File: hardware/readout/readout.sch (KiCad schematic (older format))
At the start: 0 parts

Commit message: Schematic progress
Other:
- note added: "Each sheet represents\n6 CITIROC ASICS\neach processing 32 SiPMs"
- note added: "Each sheet represents\nOne Trenz FPGA module\nprocessing 96 SiPMs"
- note added: "Each sheet represents\ntwo backplane connectors\ncarrying 192 SiPM inputs"
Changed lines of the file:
@@
 $Descr A4 11693 8268
 encoding utf-8
-Sheet 1 9
+Sheet 1 12
 Title ""
 Date ""
@@
 EMPHATIC Readout Board
 $Sheet
-S 1050 950  1000 1000
-U 61016FDD
-F0 "96Chan.sch" 50
-F1 "96Chan.sch" 50
-F2 "TRIG[0..95]" O R 2050 1450 50
+S 1400 2000 1050 700
+U 61195331
+F0 "sheet61195329" 50
+F1 "bp192.sch" 50
+F2 "SIPM[0..191]" O R 2450 2150 50
+F3 "VDD" I L 1400 2150 50
+F4 "BIAS[1..12]" I L 1400 2450 50
+F5 "TEMP[1..4]" O R 2450 2450 50
 $EndSheet
 $Sheet
-S 2750 950  750  1000
-U 61042CB4
-F0 "trenz" 50
+S 1400 3150 1050 700
+U 61195337
+F0 "sheet6119532A" 50
+F1 "bp192.sch" 50
+F2 "SIPM[0..191]" O R 2450 3300 50
+F3 "VDD" I L 1400 3300 50
+F4 "BIAS[1..12]" I L 1400 3600 50
+F5 "TEMP[1..4]" O R 2450 3600 50
+$EndSheet
+$Sheet
+S 1400 4300 1050 700
+U 6119533D
+F0 "sheet6119532B" 50
+F1 "bp192.sch" 50
+F2 "SIPM[0..191]" O R 2450 4450 50
+F3 "VDD" I L 1400 4450 50
+F4 "BIAS[1..12]" I L 1400 4750 50
+F5 "TEMP[1..4]" O R 2450 4750 50
+$EndSheet
+$Sheet
+S 4950 1800 1250 700
+U 611955AA
+F0 "sheet611955AA" 50
 F1 "trenz.sch" 50
-F2 "TRIG[0..95]" I L 2750 1450 50
-F3 "DATA_TX_P" O R 3500 1100 50
-F4 "DATA_TX_N" O R 3500 1200 50
-F5 "DATA_RX_P" I R 3500 1650 50
-F6 "DATA_RX_N" I R 3500 1750 50
+F2 "TRIG[0..95]" I L 4950 2150 50
+F3 "DATA_TX_P" O R 6200 1950 50
+F4 "DATA_TX_N" O R 6200 2050 50
+F5 "DATA_RX_P" I R 6200 2250 50
+F6 "DATA_RX_N" I R 6200 2350 50
+$EndSheet
+$Sheet
+S 3150 2000 1200 700
+U 61098CF8
+F0 "6xCITIROC" 50
+F1 "18xCITIROC.sch" 50
+F2 "SIPM[0..191]" I L 3150 2150 50
+F3 "TRIG[0..95]" O R 4350 2150 50
+F4 "TRIG[96..191]" O R 4350 2600 50
+F5 "CCTRL[0..4]" I L 3150 2350 50
+F6 "APROBE[0..5]" O R 4350 2300 50
+F7 "DPROBE[0..5]" O R 4350 2450 50
+F8 "SRCLK[0..5]" I L 3150 2500 50
 $EndSheet
 Wire Bus Line
-	2750 1450 2050 1450
-Text Label 2200 1450 0    50   ~ 0
-TRIG[0..95]
+	2450 2150 3150 2150
+Text Label 2550 2150 0    50   ~ 0
+SIPM[0..191]
+Text Notes 1150 1300 0    75   ~ 0
+Each sheet represents\ntwo backplane connectors\ncarrying 192 SiPM inputs
+Text Notes 3050 1250 0    75   ~ 0
+Each sheet represents\n6 CITIROC ASICS\neach processing 32 SiPMs
+Text Notes 6100 1200 0    75   ~ 0
+Each sheet represents\nOne Trenz FPGA module\nprocessing 96 SiPMs
 $Sheet
-S 1050 3000 1000 2850
-U 611127F4
-F0 "backplane" 50
-F1 "backplane.sch" 50
+S 3150 3150 1200 700
+U 6109C7A4
+F0 "sheet6109C7A4" 50
+F1 "18xCITIROC.sch" 50
+F2 "SIPM[0..191]" I L 3150 3300 50
+F3 "TRIG[0..95]" O R 4350 3300 50
+F4 "TRIG[96..191]" O R 4350 3750 50
+F5 "CCTRL[0..4]" I L 3150 3500 50
+F6 "APROBE[0..5]" O R 4350 3450 50
+F7 "DPROBE[0..5]" O R 4350 3600 50
+F8 "SRCLK[0..5]" I L 3150 3650 50
 $EndSheet
+Wire Bus Line
+	2450 3300 3150 3300
+$Sheet
+S 3150 4300 1200 700
+U 6109CA1E
+F0 "sheet6109CA1E" 50
+F1 "18xCITIROC.sch" 50
+F2 "SIPM[0..191]" I L 3150 4450 50
+F3 "TRIG[0..95]" O R 4350 4450 50
+F4 "TRIG[96..191]" O R 4350 4900 50
+F5 "CCTRL[0..4]" I L 3150 4650 50
+F6 "APROBE[0..5]" O R 4350 4600 50
+F7 "DPROBE[0..5]" O R 4350 4750 50
+F8 "SRCLK[0..5]" I L 3150 4800 50
+$EndSheet
+Wire Bus Line
+	2450 4450 3150 4450
+$Sheet
+S 6850 2250 1250 700
+U 6109DB23
+F0 "sheet6109DB23" 50
+F1 "trenz.sch" 50
+F2 "TRIG[0..95]" I L 6850 2600 50
+F3 "DATA_TX_P" O R 8100 2400 50
+F4 "DATA_TX_N" O R 8100 2500 50
+F5 "DATA_RX_P" I R 8100 2700 50
+F6 "DATA_RX_N" I R 8100 2800 50
+$EndSheet
+$Sheet
+S 4950 2950 1250 700
+U 6109DD07
+F0 "sheet6109DD07" 50
+F1 "trenz.sch" 50
+F2 "TRIG[0..95]" I L 4950 3300 50
+F3 "DATA_TX_P" O R 6200 3100 50
+F4 "DATA_TX_N" O R 6200 3200 50
+F5 "DATA_RX_P" I R 6200 3400 50
+F6 "DATA_RX_N" I R 6200 3500 50
+$EndSheet
+$Sheet
+S 6850 3400 1250 700
+U 6109DD0E
+F0 "sheet6109DD0E" 50
+F1 "trenz.sch" 50
+F2 "TRIG[0..95]" I L 6850 3750 50
+F3 "DATA_TX_P" O R 8100 3550 50
+F4 "DATA_TX_N" O R 8100 3650 50
+F5 "DATA_RX_P" I R 8100 3850 50
+F6 "DATA_RX_N" I R 8100 3950 50
+$EndSheet
+$Sheet
+S 4950 4100 1250 700
+U 6109E0BA
+F0 "sheet6109E0BA" 50
+F1 "trenz.sch" 50
+F2 "TRIG[0..95]" I L 4950 4450 50
+F3 "DATA_TX_P" O R 6200 4250 50
+F4 "DATA_TX_N" O R 6200 4350 50
+F5 "DATA_RX_P" I R 6200 4550 50
+F6 "DATA_RX_N" I R 6200 4650 50
+$EndSheet
+$Sheet
+S 6850 4550 1250 700
+U 6109E0C1
+F0 "sheet6109E0C1" 50
+F1 "trenz.sch" 50
+F2 "TRIG[0..95]" I L 6850 4900 50
+F3 "DATA_TX_P" O R 8100 4700 50
+F4 "DATA_TX_N" O R 8100 4800 50
+F5 "DATA_RX_P" I R 8100 5000 50
+F6 "DATA_RX_N" I R 8100 5100 50
+$EndSheet
+Wire Bus Line
+	4350 2600 6850 2600
+Wire Bus Line
+	4350 2150 4950 2150
+Wire Bus Line
+	4350 3750 6850 3750
+Wire Bus Line
+	4350 3300 4950 3300
+Wire Bus Line
+	4350 4900 6850 4900
+Wire Bus Line
+	4350 4450 4950 4450
 $EndSCHEMATC

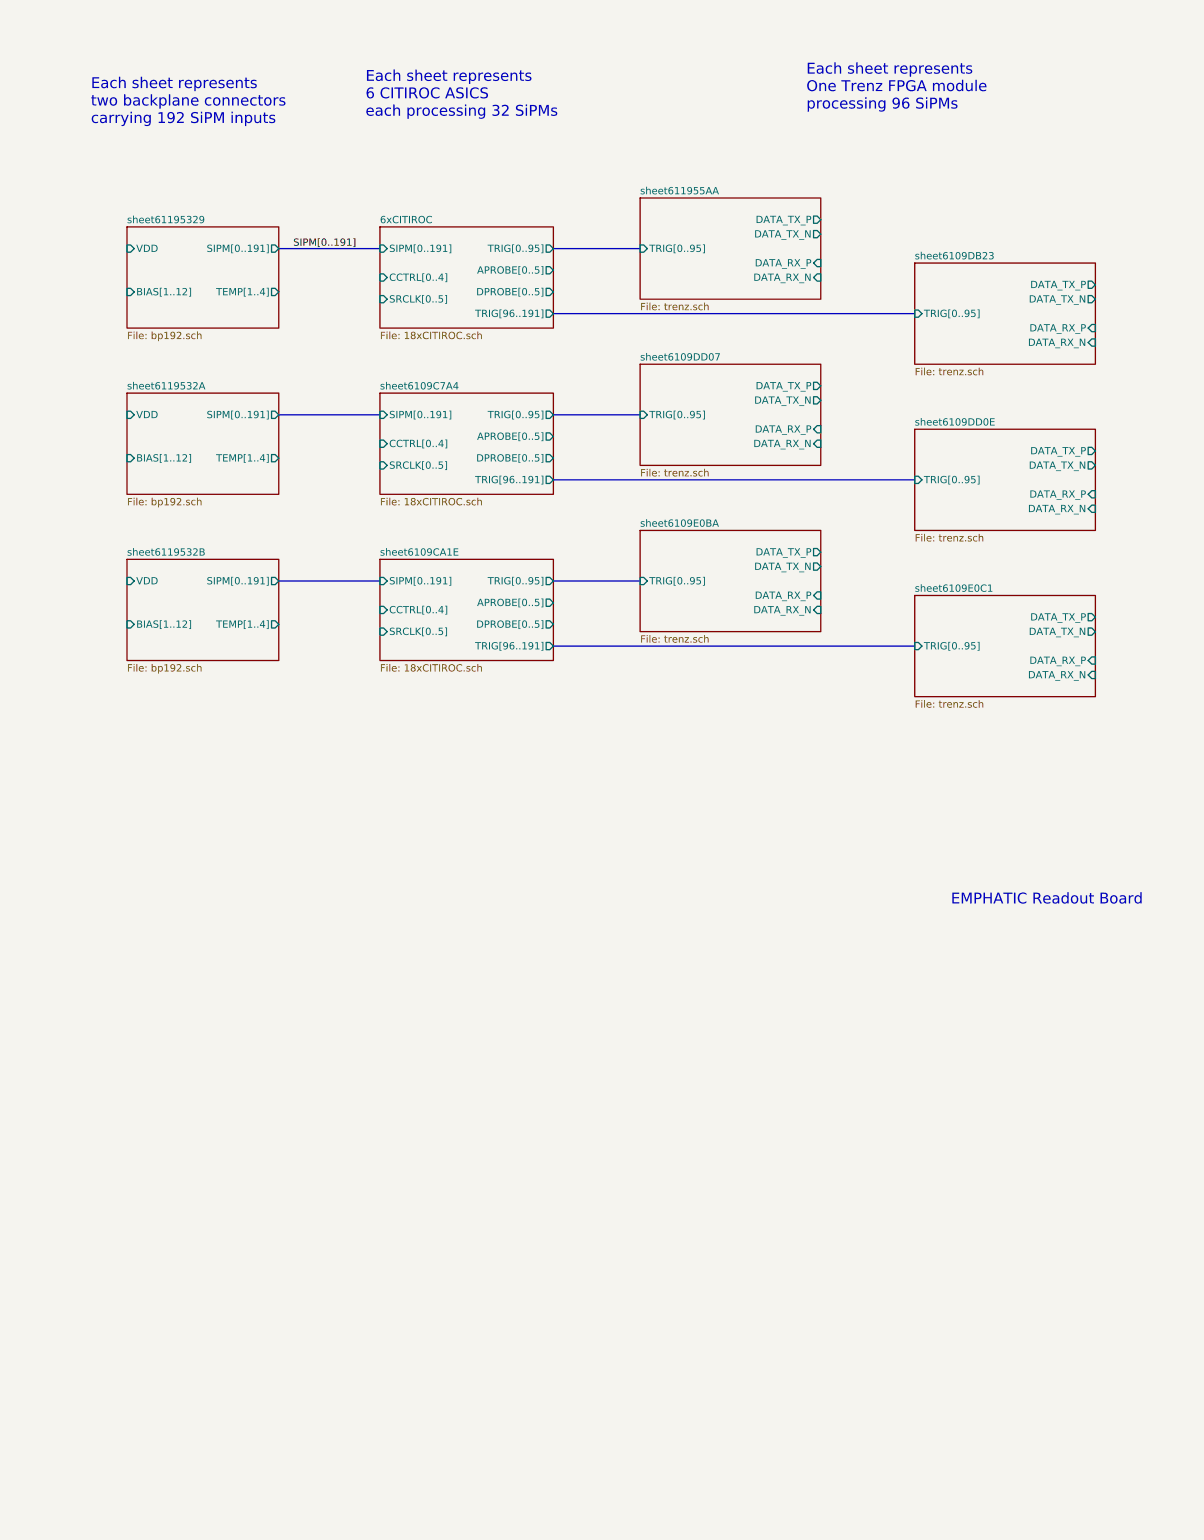
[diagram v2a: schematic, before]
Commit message: Readout schem heirarchy almost done
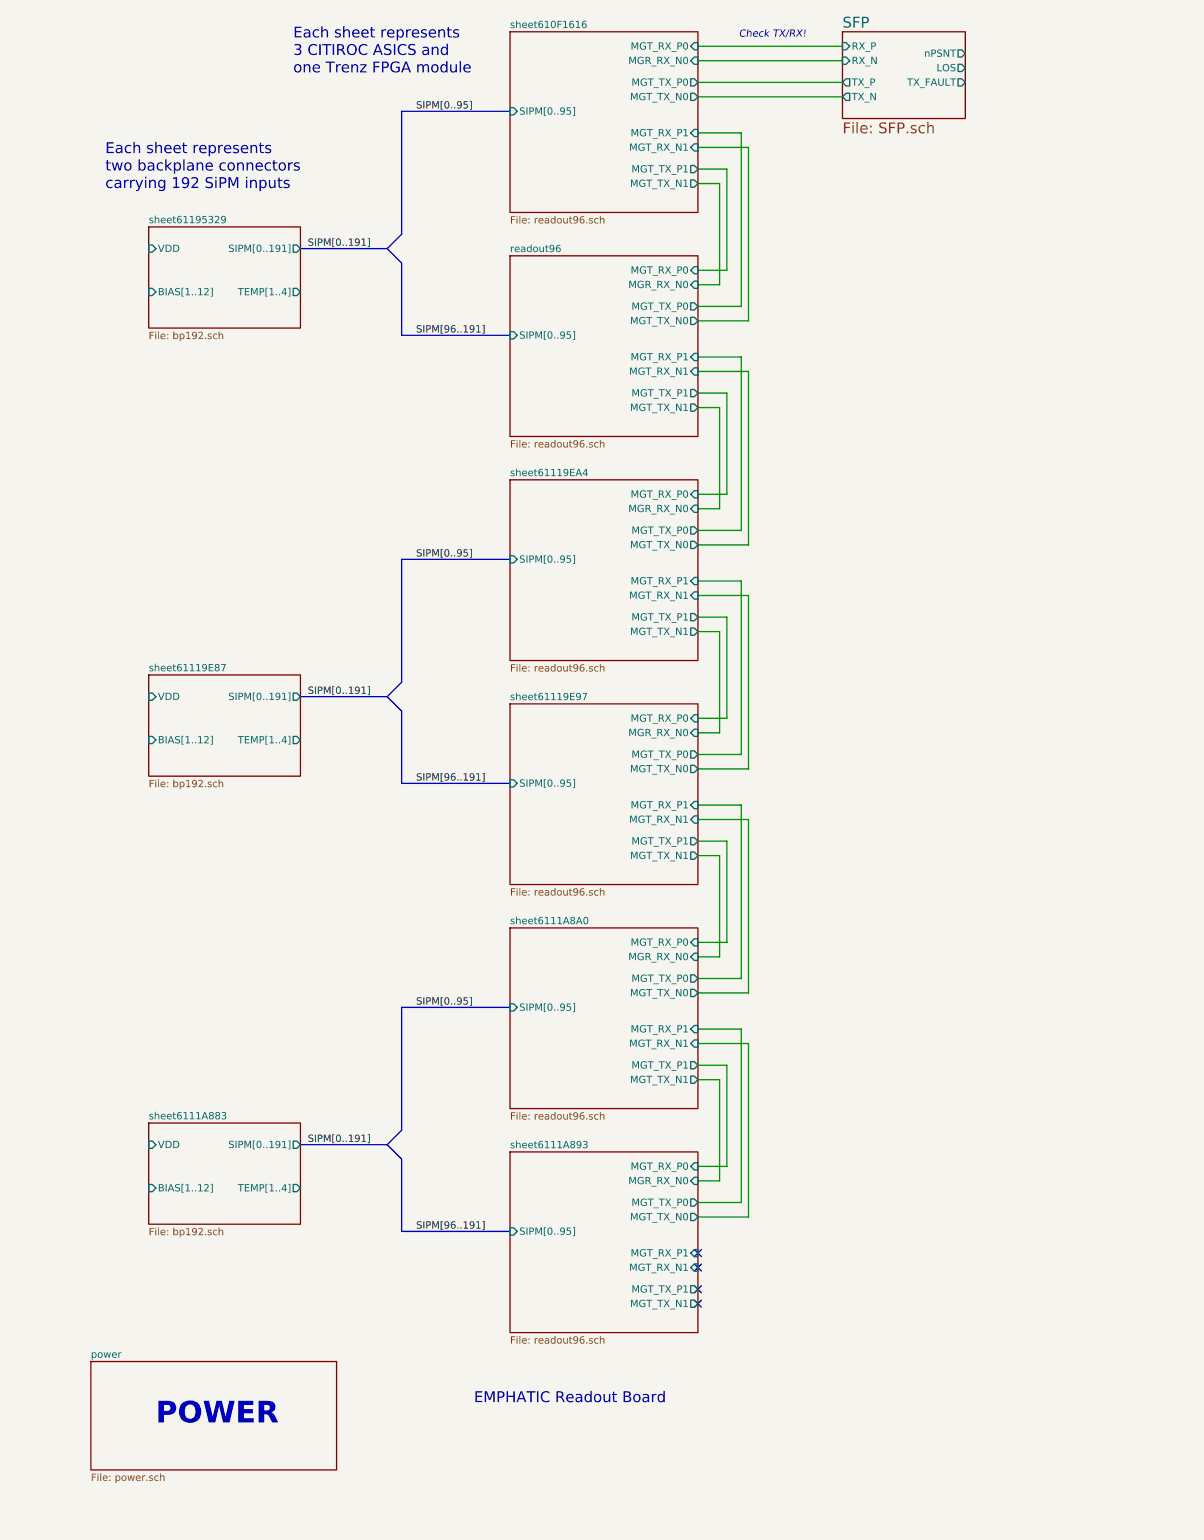
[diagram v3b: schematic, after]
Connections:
- no-connect marks 0 -> 4
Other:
- note added: "Check TX/RX!"
- note added: "Each sheet represents\n3 CITIROC ASICS and\none Trenz FPGA module"
- note added: "POWER"
- note removed: "Each sheet represents\n6 CITIROC ASICS\neach processing 32 SiPMs"
- note removed: "Each sheet represents\nOne Trenz FPGA module\nprocessing 96 SiPMs"

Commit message: schematic in progress
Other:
- note added: "EMPHATIC Readout Board\nTop level"
- note removed: "EMPHATIC Readout Board"
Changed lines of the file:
@@
 $Descr A4 8268 11693 portrait
 encoding utf-8
-Sheet 1 35
+Sheet 1 38
 Title ""
 Date ""
@@
 Comment4 ""
 $EndDescr
-Text Notes 3800 10150 0    75   ~ 0
-EMPHATIC Readout Board
+Text Notes 3800 10300 0    75   ~ 0
+EMPHATIC Readout Board\nTop level
 $Sheet
 S 1550 2000 1050 700
@@
 F5 "TEMP[1..4]" O R 2600 2450 50
 $EndSheet
-Text Notes 1250 1750 0    75   ~ 0
+Text Notes 1550 1750 0    75   ~ 0
 Each sheet represents\ntwo backplane connectors\ncarrying 192 SiPM inputs
 Text Notes 2550 950  0    75   ~ 0
@@
 F9 "MGT_TX_P1" O R 5350 3150 50
 F10 "MGT_TX_N1" O R 5350 3250 50
+F11 "CTRL[0..3]" B R 5350 2750 50
 $EndSheet
 Wire Bus Line
@@
 F9 "MGT_TX_P1" O R 5350 1600 50
 F10 "MGT_TX_N1" O R 5350 1700 50
+F11 "CTRL[0..3]" B R 5350 1200 50
 $EndSheet
 Wire Bus Line
@@
 F9 "MGT_TX_P1" O R 5350 6250 50
 F10 "MGT_TX_N1" O R 5350 6350 50
+F11 "CTRL[0..3]" B R 5350 5850 50
 $EndSheet
 Wire Bus Line
@@
 F9 "MGT_TX_P1" O R 5350 4700 50
 F10 "MGT_TX_N1" O R 5350 4800 50
+F11 "CTRL[0..3]" B R 5350 4300 50
 $EndSheet
 Wire Bus Line
@@
 F9 "MGT_TX_P1" O R 5350 9350 50
 F10 "MGT_TX_N1" O R 5350 9450 50
+F11 "CTRL[0..3]" B R 5350 8950 50
 $EndSheet
 Wire Bus Line
@@
 F9 "MGT_TX_P1" O R 5350 7800 50
 F10 "MGT_TX_N1" O R 5350 7900 50
+F11 "CTRL[0..3]" B R 5350 7400 50
 $EndSheet
 Wire Bus Line
@@
 Check TX/RX!
 $Sheet
-S 1150 9850 1700 750
+S 1200 10150 1700 750
 U 6110C8BB
 F0 "power" 50
 F1 "power.sch" 50
 $EndSheet
-Text Notes 2450 10300 2    150  ~ 30
+Text Notes 2500 10600 2    150  ~ 30
 POWER
+Wire Bus Line
+	5350 1200 6050 1200
+Wire Bus Line
+	6050 1200 6050 1750
+Text Label 6250 1750 0    50   ~ 0
+CTRL[0..3]
+Entry Wire Line
+	7600 1750 7700 1650
+Entry Wire Line
+	7450 1750 7550 1650
+Entry Wire Line
+	7300 1750 7400 1650
+Wire Wire Line
+	7700 1650 7700 800
+Wire Wire Line
+	7700 800  7200 800
+Wire Wire Line
+	7550 1650 7550 900
+Wire Wire Line
+	7550 900  7200 900
+Wire Wire Line
+	7400 1650 7400 1000
+Wire Wire Line
+	7400 1000 7200 1000
+Text Label 7400 1500 1    50   ~ 0
+CTRL2
+Text Label 7550 1500 1    50   ~ 0
+CTRL1
+Text Label 7700 1500 1    50   ~ 0
+CTRL0
+$Sheet
+S 6350 2400 850  700
+U 61157F0F
+F0 "frontpanel" 50
+F1 "frontpanel.sch" 50
+F2 "CTRL[0..3]" B L 6350 2750 50
+$EndSheet
+Wire Bus Line
+	6350 2750 5350 2750
+$Sheet
+S 800  3750 550  350
+U 6115C3E5
+F0 "bias" 75
+F1 "bias.sch" 75
+F2 "BIAS" O R 1350 3900 50
+$EndSheet
+Wire Bus Line
+	6050 1750 7600 1750
 $EndSCHEMATC

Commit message: working on schematic
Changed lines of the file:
@@
 $Descr A4 8268 11693 portrait
 encoding utf-8
-Sheet 1 38
+Sheet 1 56
 Title ""
 Date ""
@@
 	3200 2150 3300 2050
 Text Label 2650 2150 0    50   ~ 0
-SIPM[0..191]
+SIPMA[0..191]
 Entry Bus Bus
 	3300 2250 3200 2150
 Text Label 3400 2750 0    50   ~ 0
-SIPM[96..191]
+SIPMA[96..191]
 Text Label 3400 1200 0    50   ~ 0
-SIPM[0..95]
+SIPMA[0..95]
 $Sheet
 S 4050 2200 1300 1250
@@
 	3200 5250 3300 5150
 Text Label 2650 5250 0    50   ~ 0
-SIPM[0..191]
+SIPMB[0..191]
 Entry Bus Bus
 	3300 5350 3200 5250
 Text Label 3400 5850 0    50   ~ 0
-SIPM[96..191]
+SIPMB[96..191]
 Text Label 3400 4300 0    50   ~ 0
-SIPM[0..95]
+SIPMB[0..95]
 $Sheet
 S 4050 5300 1300 1250
@@
 	3200 8350 3300 8250
 Text Label 2650 8350 0    50   ~ 0
-SIPM[0..191]
+SIPMC[0..191]
 Entry Bus Bus
 	3300 8450 3200 8350
 Text Label 3400 8950 0    50   ~ 0
-SIPM[96..191]
+SIPMC[96..191]
 Text Label 3400 7400 0    50   ~ 0
-SIPM[0..95]
+SIPMC[0..95]
 $Sheet
 S 4050 8400 1300 1250

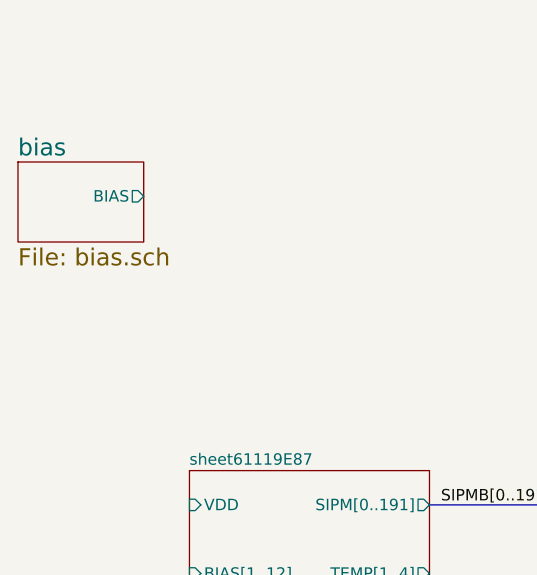
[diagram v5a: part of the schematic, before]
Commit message: schematic update
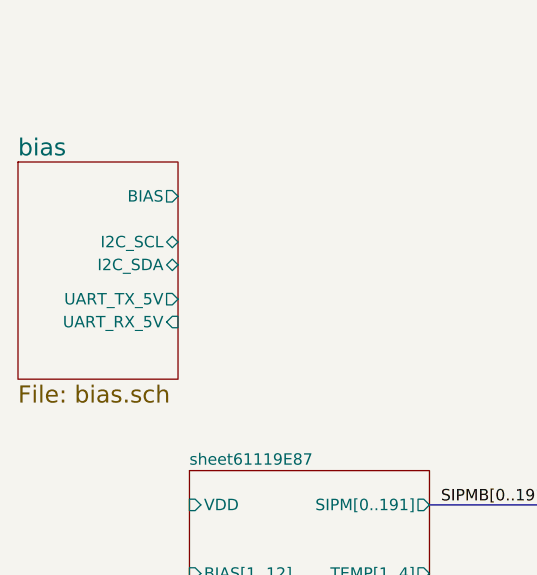
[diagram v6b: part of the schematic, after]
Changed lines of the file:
@@
 	6350 2750 5350 2750
 $Sheet
-S 800  3750 550  350
+S 800  3750 700  950
 U 6115C3E5
 F0 "bias" 75
 F1 "bias.sch" 75
-F2 "BIAS" O R 1350 3900 50
+F2 "BIAS" O R 1500 3900 50
+F3 "I2C_SCL" B R 1500 4100 50
+F4 "I2C_SDA" B R 1500 4200 50
+F5 "UART_TX_5V" O R 1500 4350 50
+F6 "UART_RX_5V" I R 1500 4450 50
 $EndSheet
 Wire Bus Line

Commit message: working on schematic
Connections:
- net labels added: CTRL10, CTRL11, CTRL8, CTRL9, CTRL[0..11], CTRL[4..7], CTRL[8..11], TEMP[0..2], TEMP[0..8], TEMP[3..5], TEMP[6..8]
- wire segments 70 -> 85
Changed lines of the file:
@@
 F1 "bp192.sch" 50
 F2 "SIPM[0..191]" O R 2600 2150 50
-F3 "VDD" I L 1550 2150 50
-F4 "BIAS[1..12]" I L 1550 2450 50
-F5 "TEMP[1..4]" O R 2600 2450 50
+F3 "TEMP[1..3]" O R 2600 2450 50
+F4 "BIAS" I L 1550 2150 50
 $EndSheet
 Text Notes 1550 1750 0    75   ~ 0
@@
 F9 "MGT_TX_P1" O R 5350 3150 50
 F10 "MGT_TX_N1" O R 5350 3250 50
-F11 "CTRL[0..3]" B R 5350 2750 50
+F11 "CTRL[0..7]" B R 5350 2750 50
 $EndSheet
 Wire Bus Line
@@
 F9 "MGT_TX_P1" O R 5350 1600 50
 F10 "MGT_TX_N1" O R 5350 1700 50
-F11 "CTRL[0..3]" B R 5350 1200 50
+F11 "CTRL[0..11]" B R 5350 1200 50
 $EndSheet
 Wire Bus Line
@@
 F1 "bp192.sch" 50
 F2 "SIPM[0..191]" O R 2600 5250 50
-F3 "VDD" I L 1550 5250 50
-F4 "BIAS[1..12]" I L 1550 5550 50
-F5 "TEMP[1..4]" O R 2600 5550 50
+F3 "TEMP[1..3]" O R 2600 5550 50
+F4 "BIAS" I L 1550 5250 50
 $EndSheet
 Entry Bus Bus
@@
 F1 "bp192.sch" 50
 F2 "SIPM[0..191]" O R 2600 8350 50
-F3 "VDD" I L 1550 8350 50
-F4 "BIAS[1..12]" I L 1550 8650 50
-F5 "TEMP[1..4]" O R 2600 8650 50
+F3 "TEMP[1..3]" O R 2600 8650 50
+F4 "BIAS" I L 1550 8350 50
 $EndSheet
 Entry Bus Bus
@@
 Wire Bus Line
 	5350 1200 6050 1200
-Wire Bus Line
-	6050 1200 6050 1750
-Text Label 6250 1750 0    50   ~ 0
+Text Label 6200 1750 0    50   ~ 0
 CTRL[0..3]
 Entry Wire Line
@@
 CTRL0
 $Sheet
-S 6350 2400 850  700
+S 1100 3350 700  950
+U 6115C3E5
+F0 "bias" 75
+F1 "bias.sch" 75
+F2 "BIAS" O R 1800 3500 50
+F3 "I2C_SCL" B R 1800 3700 50
+F4 "I2C_SDA" B R 1800 3800 50
+F5 "UART_TX" O R 1800 3950 50
+F6 "UART_RX" I R 1800 4050 50
+F7 "T[0..8]" I L 1100 3500 50
+$EndSheet
+Wire Wire Line
+	1800 3500 2000 3500
+Wire Wire Line
+	2000 3500 2000 3000
+Wire Wire Line
+	2000 3000 1350 3000
+Wire Wire Line
+	1350 3000 1350 2150
+Wire Wire Line
+	1350 2150 1550 2150
+Wire Wire Line
+	2000 3500 2000 4800
+Wire Wire Line
+	2000 4800 1300 4800
+Wire Wire Line
+	1300 4800 1300 5250
+Wire Wire Line
+	1300 5250 1550 5250
+Connection ~ 2000 3500
+Wire Wire Line
+	1300 5250 1300 8350
+Wire Wire Line
+	1300 8350 1550 8350
+Connection ~ 1300 5250
+$Sheet
+S 7000 2400 550  700
 U 61157F0F
 F0 "frontpanel" 50
 F1 "frontpanel.sch" 50
-F2 "CTRL[0..3]" B L 6350 2750 50
-$EndSheet
-Wire Bus Line
-	6350 2750 5350 2750
-$Sheet
-S 800  3750 700  950
-U 6115C3E5
-F0 "bias" 75
-F1 "bias.sch" 75
-F2 "BIAS" O R 1500 3900 50
-F3 "I2C_SCL" B R 1500 4100 50
-F4 "I2C_SDA" B R 1500 4200 50
-F5 "UART_TX_5V" O R 1500 4350 50
-F6 "UART_RX_5V" I R 1500 4450 50
-$EndSheet
-Wire Bus Line
-	6050 1750 7600 1750
+F2 "CTRL[0..3]" B L 7000 2750 50
+$EndSheet
+Entry Bus Bus
+	6050 1650 6150 1750
+Entry Bus Bus
+	6050 1850 6150 1950
+Text Label 5450 1200 0    50   ~ 0
+CTRL[0..11]
+Text Label 6200 1950 0    50   ~ 0
+CTRL[4..7]
+Wire Bus Line
+	6150 1950 6850 1950
+Wire Bus Line
+	6850 1950 6850 2750
+Wire Bus Line
+	6850 2750 7000 2750
+Entry Bus Bus
+	6050 2100 6150 2200
+Wire Bus Line
+	6150 2200 6500 2200
+Text Label 6200 2200 0    50   ~ 0
+CTRL[8..11]
+Wire Wire Line
+	1800 3700 2700 3700
+Wire Wire Line
+	1800 3800 2700 3800
+Text Label 2150 3700 0    50   ~ 0
+CTRL8
+Text Label 2150 3800 0    50   ~ 0
+CTRL9
+Wire Wire Line
+	1800 3950 2700 3950
+Wire Wire Line
+	1800 4050 2700 4050
+Text Label 2150 3950 0    50   ~ 0
+CTRL10
+Text Label 2150 4050 0    50   ~ 0
+CTRL11
+Wire Bus Line
+	2600 2450 3000 2450
+Text Label 2700 2450 0    50   ~ 0
+TEMP[0..2]
+Wire Bus Line
+	2600 5550 3000 5550
+Text Label 2700 5550 0    50   ~ 0
+TEMP[3..5]
+Wire Bus Line
+	2600 8650 3050 8650
+Text Label 2700 8650 0    50   ~ 0
+TEMP[6..8]
+Wire Bus Line
+	1100 3500 600  3500
+Wire Bus Line
+	6150 1750 7600 1750
+Wire Bus Line
+	6050 1200 6050 2100
+Text Label 600  3500 0    50   ~ 0
+TEMP[0..8]
 $EndSCHEMATC
